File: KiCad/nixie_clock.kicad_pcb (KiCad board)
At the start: 2 copper layers, 33 parts, among them Q1 2SA1015, Q2 2SK3234, U1 ESP32-DevKitC, U2 TLP627-2, U3 SN74141, U4 TLP627-2, U5 TLP627-2, U6 NJM2360A, U7 NJM7805S

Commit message: change schematics
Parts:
- added D3, D4, D5, D6, D7, D8: LED, LEDs:LED_0603, F.Cu at (232.4, 130.8)
- added NT1: IN-12B, nixie_clock:IN-12, F.Cu at (71.1, 38.1)
- added NT2: IN-12B, nixie_clock:IN-12, F.Cu at (94.0, 38.1)
- added NT3: IN-12B, nixie_clock:IN-12, F.Cu at (116.8, 38.1)
- added NT4: IN-12B, nixie_clock:IN-12, F.Cu at (139.7, 38.1)
- added NT5: IN-12B, nixie_clock:IN-12, F.Cu at (162.6, 38.1)
- added NT6: IN-12B, nixie_clock:IN-12, F.Cu at (48.3, 38.1)
- added R14, R15, R16, R17, R18, R19: 300, Resistors_SMD:R_0603, F.Cu at (232.4, 130.8)
- R1, R3, R4, R5, R6, R7: footprint Resistors_ThroughHole:R_Axial_DIN0207_L6.3mm_D2.5mm_P10.16mm_Horizontal -> Resistors_SMD:R_0603
- moved R7 93.3 mm to (240.0, 120.7)
- moved R6 92.8 mm to (240.0, 120.7)
- moved R1 47.4 mm to (240.0, 120.7)
- moved R4 47.0 mm to (240.0, 120.7)
- moved U1 38.1 mm to (204.5, 53.3)
- moved R5 33.0 mm to (240.0, 120.7)
- moved R2 25.7 mm to (231.1, 105.4)
- moved R3 20.1 mm to (240.0, 120.7)
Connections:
- U1 pad 29: Net-(U1-Pad29) -> led5
- U1 pad 30: Net-(U1-Pad30) -> led4
- U1 pad 31: Net-(U1-Pad31) -> led3
- U1 pad 33: Net-(U1-Pad33) -> led2
- U1 pad 36: Net-(U1-Pad36) -> led1
- U1 pad 37: Net-(U1-Pad37) -> led0

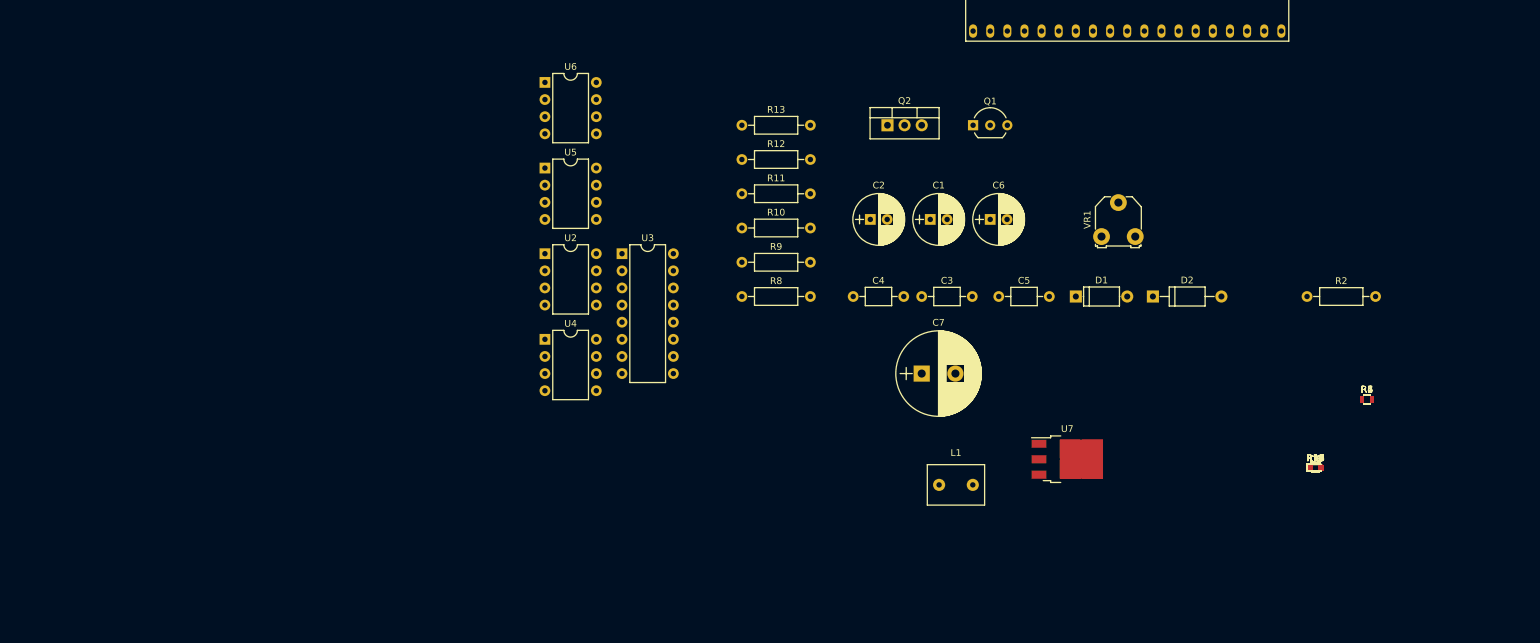
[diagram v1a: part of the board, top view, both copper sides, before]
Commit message: change some pcb packages
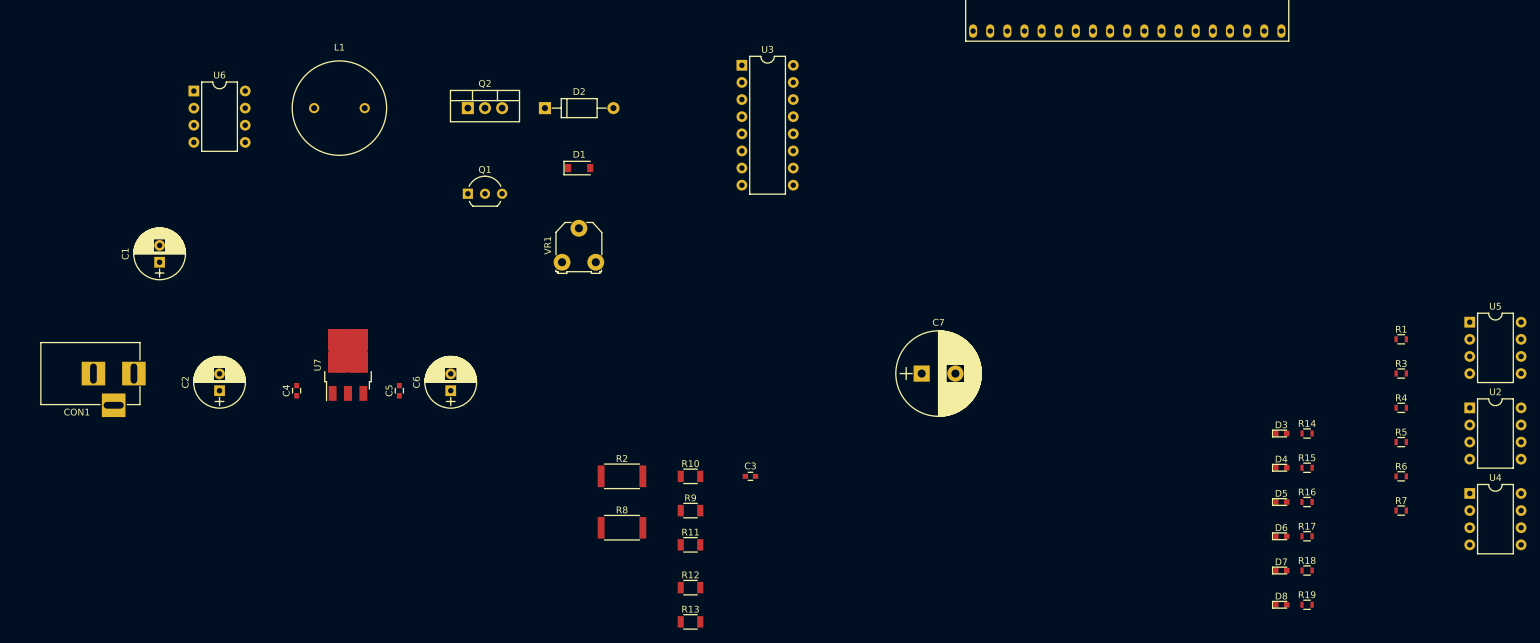
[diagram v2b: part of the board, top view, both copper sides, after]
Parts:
- added CON1: BARREL_JACK, Connect:BARREL_JACK, F.Cu at (57.1, 116.8)
- C3, C4, C5: footprint Capacitors_ThroughHole:C_Axial_L3.8mm_D2.6mm_P7.50mm_Horizontal -> Capacitors_SMD:C_0603
- D1: value 1N4148 -> 1N4148W; footprint Diodes_ThroughHole:D_A-405_P7.62mm_Horizontal -> Diodes_SMD:D_SOD-123
- L1: value 470u -> LHL13NB471K; footprint Inductors_NEOSID:Neosid_Inductor_MA-Bs75 -> nixie_clock:LHL13NB471K
- R10, R11, R12, R13, R9: footprint Resistors_ThroughHole:R_Axial_DIN0207_L6.3mm_D2.5mm_P10.16mm_Horizontal -> Resistors_SMD:R_1206
- R2, R8: footprint Resistors_ThroughHole:R_Axial_DIN0207_L6.3mm_D2.5mm_P10.16mm_Horizontal -> Resistors_SMD:R_2512
- moved U2 139.1 mm to (255.3, 121.9)
- moved U4 139.1 mm to (255.3, 134.6)
- moved U5 139.1 mm to (255.3, 109.2)
- moved C1 114.5 mm to (61.0, 100.3), turned to 90 degrees
- moved U7 107.6 mm to (88.9, 115.6), turned to 90 degrees
- moved L1 107.2 mm to (87.6, 77.5)
- moved R2 105.0 mm to (129.5, 132.1)
- moved C2 99.8 mm to (69.8, 119.4), turned to 90 degrees
- moved D2 94.4 mm to (118.1, 77.5)
- moved C5 90.0 mm to (96.5, 119.4), turned to 90 degrees
- moved C6 83.9 mm to (104.1, 119.4), turned to 90 degrees
- moved C4 83.7 mm to (81.3, 119.4), turned to 90 degrees
- moved VR1 80.1 mm to (120.7, 100.3)
- moved D1 76.1 mm to (123.2, 86.4)
- moved Q1 75.6 mm to (106.7, 90.2)
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
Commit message: change footprints
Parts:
- moved U1 12.8 mm to (217.2, 52.1)

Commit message: many changes
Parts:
- added NT10: IN-3, nixie_clock:IN-3, F.Cu at (102.9, 30.5)
- added NT7: IN-3, nixie_clock:IN-3, F.Cu at (125.7, 30.5)
- added NT8: IN-3, nixie_clock:IN-3, F.Cu at (118.1, 30.5)
- added NT9: IN-3, nixie_clock:IN-3, F.Cu at (110.5, 30.5)
- added R20: 300, Resistors_SMD:R_0603, F.Cu at (250.2, 121.9)
- added R21: 100k, Resistors_SMD:R_2512, F.Cu at (231.1, 124.5)
- added R22: 300, Resistors_SMD:R_0603, F.Cu at (254.0, 121.9)
- added R23: 100k, Resistors_SMD:R_2512, F.Cu at (231.1, 132.1)
- added R24: 1, Resistors_SMD:R_2512, F.Cu at (231.1, 116.8)
- added R25: 1k, Resistors_SMD:R_1206, F.Cu at (259.1, 121.9)
- added R26: 470, Resistors_SMD:R_1206, F.Cu at (264.2, 121.9)
- added R27: 470k, Resistors_SMD:R_1206, F.Cu at (269.2, 121.9)
- added R28: 470, Resistors_SMD:R_1206, F.Cu at (274.3, 121.9)
- added R29: 1k, Resistors_SMD:R_1206, F.Cu at (279.4, 121.9)
- added U8: NJM2360A, Housings_DIP:DIP-8_W7.62mm, F.Cu at (64.8, 101.6)
- added U9: NJM7805S, TO_SOT_Packages_SMD:TO-252-3_TabPin2, F.Cu at (38.1, 85.1)
- C2: value 47u -> 10u/400V; footprint Capacitors_ThroughHole:CP_Radial_D7.5mm_P2.50mm -> Capacitors_ThroughHole:CP_Radial_D12.5mm_P5.00mm
- C4: value 0.1u -> 47u; footprint Capacitors_SMD:C_0603 -> Capacitors_ThroughHole:CP_Radial_D7.5mm_P2.50mm
- C6: value 47u -> 0.1u; footprint Capacitors_ThroughHole:CP_Radial_D7.5mm_P2.50mm -> Capacitors_SMD:C_0603
- C7: value 10u/400V -> 47u; footprint Capacitors_ThroughHole:CP_Radial_D12.5mm_P5.00mm -> Capacitors_ThroughHole:CP_Radial_D7.5mm_P2.50mm
- D1: value 1N4148W -> LED; footprint Diodes_SMD:D_SOD-123 -> LEDs:LED_0603
- D2: value UF2010 -> LED; footprint Diodes_ThroughHole:D_A-405_P10.16mm_Horizontal -> LEDs:LED_0603
- D7: value LED -> UF2010; footprint LEDs:LED_0603 -> Diodes_ThroughHole:D_A-405_P10.16mm_Horizontal
- D8: value LED -> 1N4148W; footprint LEDs:LED_0603 -> Diodes_SMD:D_SOD-123
- Q1: value 2SA1015 -> 2SK3234; footprint TO_SOT_Packages_THT:TO-92_Inline_Wide -> TO_SOT_Packages_THT:TO-220-3_Vertical
- Q2: value 2SK3234 -> 2SA1015; footprint TO_SOT_Packages_THT:TO-220-3_Vertical -> TO_SOT_Packages_THT:TO-92_Inline_Wide
- R1, R3, R4, R5, R6: value 300 -> 20k; footprint Resistors_SMD:R_0603 -> Resistors_SMD:R_2512
- R10: value 470 -> 300; footprint Resistors_SMD:R_1206 -> Resistors_SMD:R_0603
- R11, R9: value 1k -> 300; footprint Resistors_SMD:R_1206 -> Resistors_SMD:R_0603
- R12: value 470k -> 300; footprint Resistors_SMD:R_1206 -> Resistors_SMD:R_0603
- R13: value 470 -> 300
- R8: value 1 -> 300; footprint Resistors_SMD:R_2512 -> Resistors_SMD:R_0603
- U3: value SN74141 -> TLP627-2; footprint Housings_DIP:DIP-16_W7.62mm -> Housings_DIP:DIP-8_W7.62mm
- U5: value TLP627-2 -> SN74141; footprint Housings_DIP:DIP-8_W7.62mm -> Housings_DIP:DIP-16_W7.62mm
- U6: value NJM2360A -> TLP627; footprint Housings_DIP:DIP-8_W7.62mm -> Housings_DIP:DIP-4_W7.62mm
- U7: value NJM7805S -> TLP627-2; footprint TO_SOT_Packages_SMD:TO-252-3_TabPin2 -> Housings_DIP:DIP-8_W7.62mm
- moved U5 232.5 mm to (22.9, 101.6)
- moved U2 216.9 mm to (39.4, 101.6)
- moved U4 216.7 mm to (39.4, 115.6)
- moved U1 209.3 mm to (35.6, 156.2), turned to 90 degrees
- moved NT1 197.4 mm to (268.0, 22.9)
- moved NT2 151.9 mm to (245.1, 22.9)
- moved C1 141.3 mm to (201.9, 90.2), turned to 0 degrees
- moved R12 126.0 mm to (261.6, 116.8)
- moved C2 121.7 mm to (188.0, 90.2), turned to 0 degrees
- moved R11 120.8 mm to (257.8, 116.8)
- moved R8 119.1 mm to (246.4, 116.8)
- moved R10 115.3 mm to (254.0, 116.8)
- moved R9 112.3 mm to (250.2, 116.8)
- moved NT3 106.5 mm to (222.2, 22.9)
- moved NT6 106.5 mm to (153.7, 22.9)
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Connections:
- C2 pad 1: +9V -> VNXE
- C5 pad 1: +5V -> +9V
- C7 pad 1: VNXE -> +5V
- D1 pad 1: Net-(D1-Pad1) -> led0
- D2 pad 1: VNXE -> led1
- D3 pad 1: led0 -> led2
- D4 pad 1: led1 -> led3
- D5 pad 1: led2 -> led4
- D6 pad 1: led3 -> led5
- D7 pad 1: led4 -> VNXE
- D8 pad 1: led5 -> Net-(D8-Pad1)
- L1 pad 2: Net-(D2-Pad2) -> Net-(D7-Pad2)
- NT2 pad 12: Net-(NT2-Pad12) -> Net-(NT1-Pad12)
- NT3 pad 12: Net-(NT3-Pad12) -> Net-(NT1-Pad12)
- NT4 pad 12: Net-(NT4-Pad12) -> Net-(NT1-Pad12)
- NT5 pad 12: Net-(NT5-Pad12) -> Net-(NT1-Pad12)
- NT6 pad 12: Net-(NT6-Pad12) -> Net-(NT1-Pad12)
- Q1 pad 1: Net-(D1-Pad1) -> Net-(D8-Pad1)
- Q1 pad 2: GND -> Net-(D7-Pad2)
- Q1 pad 3: Net-(D1-Pad2) -> GND
- Q2 pad 1: Net-(D1-Pad1) -> Net-(D8-Pad1)
- Q2 pad 2: Net-(D2-Pad2) -> GND
- Q2 pad 3: GND -> Net-(D8-Pad2)
- R1 pad 1: +3V3 -> VNXE
- R10 pad 1: Net-(L1-Pad1) -> +3V3
- R11 pad 1: Net-(D1-Pad2) -> +3V3
- R11 pad 2: GND -> Net-(R11-Pad2)
- R12 pad 1: VNXE -> +3V3
- R13 pad 1: Net-(R13-Pad1) -> Net-(D1-Pad2)
- R13 pad 2: GND -> +3V3
- R14 pad 1: Net-(D3-Pad2) -> Net-(D2-Pad2)
- R15 pad 1: Net-(D4-Pad2) -> Net-(D3-Pad2)
- R16 pad 1: Net-(D5-Pad2) -> Net-(D4-Pad2)
- R17 pad 1: Net-(D6-Pad2) -> Net-(D5-Pad2)
- R18 pad 1: Net-(D7-Pad2) -> Net-(D6-Pad2)
- R19 pad 1: Net-(D8-Pad2) -> +3V3
- R19 pad 2: +3V3 -> Net-(R19-Pad2)
- R2 pad 1: Net-(R2-Pad1) -> VNXE
- R2 pad 2: VNXE -> Net-(R2-Pad2)
- R3 pad 1: +3V3 -> VNXE
- R4 pad 1: +3V3 -> VNXE
- R5 pad 1: +3V3 -> VNXE
- R6 pad 1: +3V3 -> VNXE
- R8 pad 1: +9V -> +3V3
- R8 pad 2: Net-(L1-Pad1) -> Net-(R8-Pad2)
- R9 pad 1: Net-(L1-Pad1) -> +3V3
- U1 pad 11: Net-(U1-Pad11) -> nxedot
- U1 pad 12: Net-(U1-Pad12) -> nxecol0
- U1 pad 13: Net-(U1-Pad13) -> nxecol1
- U2 pad 1: Net-(R1-Pad2) -> Net-(R7-Pad2)
- U2 pad 3: Net-(R3-Pad2) -> Net-(R8-Pad2)
- U2 pad 6: Net-(R2-Pad1) -> Net-(R2-Pad2)
- U2 pad 8: Net-(R2-Pad1) -> Net-(R1-Pad2)
- U3 pad 1: Net-(NT1-Pad4) -> Net-(R9-Pad2)
- U3 pad 2: Net-(NT1-Pad3) -> nxecom2
- U3 pad 3: nxea -> Net-(R10-Pad2)
- U3 pad 4: nxed -> nxecom3
- U3 pad 5: +5V -> Net-(NT4-Pad1)
- U3 pad 6: nxeb -> Net-(R4-Pad2)
- U3 pad 7: nxec -> Net-(NT3-Pad1)
- U3 pad 8: Net-(NT1-Pad10) -> Net-(R3-Pad2)
- U4 pad 1: Net-(R4-Pad2) -> Net-(R11-Pad2)
- U4 pad 2: nxecom2 -> nxecom4
- U4 pad 3: Net-(R5-Pad2) -> Net-(R12-Pad2)
- U4 pad 4: nxecom3 -> nxecom5
- U4 pad 5: Net-(NT4-Pad1) -> Net-(NT6-Pad1)
- U4 pad 6: Net-(R2-Pad1) -> Net-(R6-Pad2)
- U4 pad 7: Net-(NT3-Pad1) -> Net-(NT5-Pad1)
- U4 pad 8: Net-(R2-Pad1) -> Net-(R5-Pad2)
- U5 pad 1: Net-(R6-Pad2) -> Net-(NT1-Pad4)
- U5 pad 2: nxecom4 -> Net-(NT1-Pad3)
- U5 pad 3: Net-(R7-Pad2) -> nxea
- U5 pad 4: nxecom5 -> nxed
- U5 pad 5: Net-(NT6-Pad1) -> +5V
- U5 pad 6: Net-(R2-Pad1) -> nxeb
- U5 pad 7: Net-(NT5-Pad1) -> nxec
- U5 pad 8: Net-(R2-Pad1) -> Net-(NT1-Pad10)
- U6 pad 1: Net-(R9-Pad2) -> Net-(R19-Pad2)
- U6 pad 2: Net-(D1-Pad2) -> nxedot
- U6 pad 3: Net-(C3-Pad1) -> GND
- U6 pad 4: GND -> Net-(NT1-Pad12)
- U7 pad 1: +9V -> Net-(R20-Pad2)
- U7 pad 2: GND -> nxecol0
- U7 pad 3: +5V -> Net-(R22-Pad2)
- VR1 pad 1: Net-(R12-Pad2) -> Net-(R27-Pad2)
- VR1 pad 2: Net-(R13-Pad1) -> Net-(R28-Pad1)
- VR1 pad 3: Net-(U6-Pad5) -> Net-(U8-Pad5)

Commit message: add connectors
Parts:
- added P1: CONN_02X05, Socket_Strips:Socket_Strip_Straight_2x05_Pitch2.54mm, F.Cu at (70.5, 48.5)
- added P2: CONN_02X05, Socket_Strips:Socket_Strip_Straight_2x05_Pitch2.54mm, F.Cu at (108.5, 90.5)
- added P3: CONN_02X05, Socket_Strips:Socket_Strip_Straight_2x05_Pitch2.54mm, F.Cu at (238.0, 49.0)
- added P4: CONN_02X05, Socket_Strips:Socket_Strip_Straight_2x05_Pitch2.54mm, F.Cu at (145.0, 90.5)
- Q1: footprint TO_SOT_Packages_THT:TO-220-3_Vertical -> TO_SOT_Packages_THT:TO-220-3_Horizontal
- R13: footprint Resistors_SMD:R_1206 -> Resistors_SMD:R_0603
- moved NT1 185.4 mm to (83.8, 44.5)
- moved NT2 138.8 mm to (108.0, 44.5)
- moved R14 132.8 mm to (154.9, 190.5)
- moved R15 132.8 mm to (158.8, 190.5)
- moved R16 132.8 mm to (162.6, 190.5)
- moved R17 132.8 mm to (166.4, 190.5)
- moved R18 99.7 mm to (170.2, 190.5)
- moved D7 98.6 mm to (231.1, 156.2)
- moved D8 98.6 mm to (246.4, 156.2)
- moved L1 98.6 mm to (265.4, 142.2)
- moved U8 84.7 mm to (106.7, 175.3)
- moved U6 80.1 mm to (118.1, 175.3)
- moved C3 79.1 mm to (231.1, 109.2)
- moved C5 79.1 mm to (234.9, 109.2)
- moved C6 79.1 mm to (238.8, 109.2)
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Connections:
- NT1 pad 1: Net-(NT1-Pad1) -> /nixie/nc0
- NT1 pad 10: Net-(NT1-Pad10) -> /nixie/n2
- NT1 pad 11: Net-(NT1-Pad11) -> /nixie/n1
- NT1 pad 12: Net-(NT1-Pad12) -> /nixie/ndot
- NT1 pad 2: Net-(NT1-Pad2) -> /nixie/n0
- NT1 pad 3: Net-(NT1-Pad3) -> /nixie/n9
- NT1 pad 4: Net-(NT1-Pad4) -> /nixie/n8
- NT1 pad 5: Net-(NT1-Pad5) -> /nixie/n7
- NT1 pad 6: Net-(NT1-Pad6) -> /nixie/n6
- NT1 pad 7: Net-(NT1-Pad7) -> /nixie/n5
- NT1 pad 8: Net-(NT1-Pad8) -> /nixie/n4
- NT1 pad 9: Net-(NT1-Pad9) -> /nixie/n3
- NT10 pad 1: Net-(NT10-Pad1) -> /nixie/ncol1
- NT2 pad 1: Net-(NT2-Pad1) -> /nixie/nc1
- NT2 pad 10: Net-(NT1-Pad10) -> /nixie/n2
- NT2 pad 11: Net-(NT1-Pad11) -> /nixie/n1
- NT2 pad 12: Net-(NT1-Pad12) -> /nixie/ndot
- NT2 pad 2: Net-(NT1-Pad2) -> /nixie/n0
- NT2 pad 3: Net-(NT1-Pad3) -> /nixie/n9
- NT2 pad 4: Net-(NT1-Pad4) -> /nixie/n8
- NT2 pad 5: Net-(NT1-Pad5) -> /nixie/n7
- NT2 pad 6: Net-(NT1-Pad6) -> /nixie/n6
- NT2 pad 7: Net-(NT1-Pad7) -> /nixie/n5
- NT2 pad 8: Net-(NT1-Pad8) -> /nixie/n4
- NT2 pad 9: Net-(NT1-Pad9) -> /nixie/n3
- NT3 pad 1: Net-(NT3-Pad1) -> /nixie/nc2
- NT3 pad 10: Net-(NT1-Pad10) -> /nixie/n2
- NT3 pad 11: Net-(NT1-Pad11) -> /nixie/n1
- NT3 pad 12: Net-(NT1-Pad12) -> /nixie/ndot
- NT3 pad 2: Net-(NT1-Pad2) -> /nixie/n0
- NT3 pad 3: Net-(NT1-Pad3) -> /nixie/n9
- NT3 pad 4: Net-(NT1-Pad4) -> /nixie/n8
- NT3 pad 5: Net-(NT1-Pad5) -> /nixie/n7
- NT3 pad 6: Net-(NT1-Pad6) -> /nixie/n6
- NT3 pad 7: Net-(NT1-Pad7) -> /nixie/n5
- NT3 pad 8: Net-(NT1-Pad8) -> /nixie/n4
- NT3 pad 9: Net-(NT1-Pad9) -> /nixie/n3
- NT4 pad 1: Net-(NT4-Pad1) -> /nixie/nc3
- NT4 pad 10: Net-(NT1-Pad10) -> /nixie/n2
- NT4 pad 11: Net-(NT1-Pad11) -> /nixie/n1
- NT4 pad 12: Net-(NT1-Pad12) -> /nixie/ndot
- NT4 pad 2: Net-(NT1-Pad2) -> /nixie/n0
- NT4 pad 3: Net-(NT1-Pad3) -> /nixie/n9
- NT4 pad 4: Net-(NT1-Pad4) -> /nixie/n8
- NT4 pad 5: Net-(NT1-Pad5) -> /nixie/n7
- NT4 pad 6: Net-(NT1-Pad6) -> /nixie/n6
- NT4 pad 7: Net-(NT1-Pad7) -> /nixie/n5
- NT4 pad 8: Net-(NT1-Pad8) -> /nixie/n4
- NT4 pad 9: Net-(NT1-Pad9) -> /nixie/n3
- NT5 pad 1: Net-(NT5-Pad1) -> /nixie/nc4
- NT5 pad 10: Net-(NT1-Pad10) -> /nixie/n2
- NT5 pad 11: Net-(NT1-Pad11) -> /nixie/n1
- NT5 pad 12: Net-(NT1-Pad12) -> /nixie/ndot
- NT5 pad 2: Net-(NT1-Pad2) -> /nixie/n0
- NT5 pad 3: Net-(NT1-Pad3) -> /nixie/n9
- NT5 pad 4: Net-(NT1-Pad4) -> /nixie/n8
- NT5 pad 5: Net-(NT1-Pad5) -> /nixie/n7
- NT5 pad 6: Net-(NT1-Pad6) -> /nixie/n6
- NT5 pad 7: Net-(NT1-Pad7) -> /nixie/n5
- NT5 pad 8: Net-(NT1-Pad8) -> /nixie/n4
- NT5 pad 9: Net-(NT1-Pad9) -> /nixie/n3
- NT6 pad 1: Net-(NT6-Pad1) -> /nixie/nc5
- NT6 pad 10: Net-(NT1-Pad10) -> /nixie/n2
- NT6 pad 11: Net-(NT1-Pad11) -> /nixie/n1
- NT6 pad 12: Net-(NT1-Pad12) -> /nixie/ndot
- NT6 pad 2: Net-(NT1-Pad2) -> /nixie/n0
- NT6 pad 3: Net-(NT1-Pad3) -> /nixie/n9
- NT6 pad 4: Net-(NT1-Pad4) -> /nixie/n8
- NT6 pad 5: Net-(NT1-Pad5) -> /nixie/n7
- NT6 pad 6: Net-(NT1-Pad6) -> /nixie/n6
- NT6 pad 7: Net-(NT1-Pad7) -> /nixie/n5
- NT6 pad 8: Net-(NT1-Pad8) -> /nixie/n4
- NT6 pad 9: Net-(NT1-Pad9) -> /nixie/n3
- NT8 pad 1: Net-(NT8-Pad1) -> /nixie/ncol0
- U2 pad 5: Net-(NT2-Pad1) -> /nixie/nmc1
- U2 pad 7: Net-(NT1-Pad1) -> /nixie/nmc0
- U3 pad 5: Net-(NT4-Pad1) -> /nixie/nmc3
- U3 pad 7: Net-(NT3-Pad1) -> /nixie/nmc2
- U4 pad 5: Net-(NT6-Pad1) -> /nixie/nmc5
- U4 pad 7: Net-(NT5-Pad1) -> /nixie/nmc4
- U5 pad 1: Net-(NT1-Pad4) -> /nixie/nm8
- U5 pad 10: Net-(NT1-Pad5) -> /nixie/nm7
- U5 pad 11: Net-(NT1-Pad6) -> /nixie/nm6
- U5 pad 13: Net-(NT1-Pad8) -> /nixie/nm4
- U5 pad 14: Net-(NT1-Pad7) -> /nixie/nm5
- U5 pad 15: Net-(NT1-Pad11) -> /nixie/nm1
- U5 pad 16: Net-(NT1-Pad2) -> /nixie/nm0
- U5 pad 2: Net-(NT1-Pad3) -> /nixie/nm9
- U5 pad 8: Net-(NT1-Pad10) -> /nixie/nm2
- U5 pad 9: Net-(NT1-Pad9) -> /nixie/nm3
- U6 pad 4: Net-(NT1-Pad12) -> /nixie/nmdot
- U7 pad 5: Net-(NT10-Pad1) -> /nixie/nmcol1
- U7 pad 7: Net-(NT8-Pad1) -> /nixie/nmcol0
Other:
- board outline added: 175.5 x 42.5 mm

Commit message: add edge cuts
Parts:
- CON1, U1: moved to B.Cu
- moved U1 313.4 mm to (348.8, 168.2), turned to 180 degrees
- moved U2 301.9 mm to (358.0, 229.5)
- moved U3 301.9 mm to (369.4, 229.5)
- moved U4 301.9 mm to (380.8, 229.5)
- moved U6 301.9 mm to (415.1, 229.5)
- moved U7 301.9 mm to (392.2, 229.5)
- moved Q1 298.4 mm to (318.6, 25.9)
- moved Q2 298.4 mm to (318.6, 47.5)
- moved U9 298.4 mm to (321.1, 34.8)
- moved U5 294.8 mm to (306.2, 159.2)
- moved CON1 215.1 mm to (225.8, 113.0), turned to 180 degrees
- moved U8 138.1 mm to (208.3, 81.8)
- moved C7 117.7 mm to (340.6, 62.8)
- moved C4 117.7 mm to (350.8, 62.8)
- moved C5 117.7 mm to (346.9, 73.0)
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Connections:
- NT7 pad 2: GND -> /nixie/ngnd
- NT9 pad 2: GND -> /nixie/ngnd
- P1 pad 10: /nixie/n0 -> /nixie/n6
- P1 pad 2: /nixie/n6 -> /nixie/n0
- P1 pad 4: /nixie/n7 -> /nixie/n9
- P1 pad 8: /nixie/n9 -> /nixie/n7
- P2 pad 10: /nixie/nm0 -> /nixie/nm6
- P2 pad 2: /nixie/nm6 -> /nixie/nm0
- P2 pad 4: /nixie/nm7 -> /nixie/nm9
- P2 pad 8: /nixie/nm9 -> /nixie/nm7
- P3 pad 1: /nixie/nc0 -> /nixie/nc4
- P3 pad 10: /nixie/nc5 -> /nixie/ngnd
- P3 pad 2: /nixie/ncol1 -> /nixie/nc5
- P3 pad 3: /nixie/nc1 -> /nixie/nc3
- P3 pad 4: /nixie/ncol0 -> /nixie/ndot
- P3 pad 6: /nixie/ndot -> /nixie/ncol1
- P3 pad 7: /nixie/nc3 -> /nixie/nc1
- P3 pad 8: Net-(P3-Pad8) -> /nixie/ncol0
- P3 pad 9: /nixie/nc4 -> /nixie/nc0
- P4 pad 1: /nixie/nmc0 -> /nixie/nmc4
- P4 pad 10: /nixie/nmc5 -> /nixie/nmgnd
- P4 pad 2: /nixie/nmcol1 -> /nixie/nmc5
- P4 pad 3: /nixie/nmc1 -> /nixie/nmc3
- P4 pad 4: /nixie/nmcol0 -> /nixie/nmdot
- P4 pad 6: /nixie/nmdot -> /nixie/nmcol1
- P4 pad 7: /nixie/nmc3 -> /nixie/nmc1
- P4 pad 8: Net-(P4-Pad8) -> /nixie/nmcol0
- P4 pad 9: /nixie/nmc4 -> /nixie/nmc0
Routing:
- net /nixie/n8: track 0.00 -> 191.5 mm
- net /nixie/n7: track 0.00 -> 187.5 mm
- net /nixie/n9: track 0.00 -> 185.1 mm
- net /nixie/nc0: track 0.00 -> 178.5 mm
- net /nixie/n6: track 0.00 -> 169.2 mm
- net /nixie/ndot: track 0.00 -> 167.8 mm
- net /nixie/n0: track 0.00 -> 167.1 mm
- net /nixie/n1: track 0.00 -> 164.4 mm
- net /nixie/n5: track 0.00 -> 163.5 mm
- net /nixie/n4: track 0.00 -> 162.7 mm
- net /nixie/n2: track 0.00 -> 161.7 mm
- net /nixie/n3: track 0.00 -> 156.5 mm
- net /nixie/nc1: track 0.00 -> 149.3 mm
- net /nixie/ncol1: track 0.00 -> 131.8 mm
- net /nixie/ngnd: track 0.00 -> 120.1 mm
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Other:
- board size 175.5 x 42.5 mm -> 186 x 100 mm
- copper layers 2 -> 4

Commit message: place components
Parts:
- C3, C5, C6, D7, D8, L1, Q1, Q2, R1, R10, R11, R12, R19, R2, R20, R21, R22, R23, R24, R25, R26, R27, R28, R29, R3, R4, R5, R6, R7, R8, R9, U2, U3, U4, U5, U6, U7, U8, U9, VR1: moved to B.Cu
- C4, C7: footprint Capacitors_ThroughHole:CP_Radial_D7.5mm_P2.50mm -> nixie_clock:C_3225; moved to B.Cu
- moved U4 273.3 mm to (138.9, 102.4)
- moved U3 270.4 mm to (138.9, 88.1)
- moved U1 267.7 mm to (88.1, 106.9)
- moved U6 267.1 mm to (171.4, 120.1)
- moved U7 259.2 mm to (157.5, 119.6)
- moved U2 247.0 mm to (138.9, 115.3)
- moved U5 234.6 mm to (83.3, 86.4), turned to 90 degrees
- moved L1 198.8 mm to (179.8, 84.3), turned to 180 degrees
- moved R29 191.1 mm to (200.4, 80.0), turned to 90 degrees
- moved R28 180.2 mm to (206.8, 100.8), turned to 90 degrees
- moved R27 177.2 mm to (204.2, 94.5)
- moved D7 170.6 mm to (174.5, 94.5)
- moved R25 167.1 mm to (204.0, 87.9)
- moved D8 161.6 mm to (200.7, 84.6)
- moved R26 156.0 mm to (220.2, 87.9)
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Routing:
- net GND: track 0.00 -> 26.7 mm
- net +5V: track 0.00 -> 6.60 mm
- net +9V: track 0.00 -> 6.35 mm
